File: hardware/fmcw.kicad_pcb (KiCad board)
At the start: 4 copper layers, 147.8 x 58.9 mm, 412 parts, among them CON1 BARREL_JACK, J1 SD_Card, J2 USB_B_Micro, J3 SMA, J4 SMA, J5 SMA, P1 CONN_02X04, P2 CONN_02X04, Q1 DNP(RE1C002UN), Q2 RE1C002UN, SW1 SW_PUSH, U1 LP5907MFX-3.3, U10 LP5907MFX-3.0, U11 LTC2292, U12 ADF4158, U13 TLV172DCK, U14 PAT1220-3dB, U15 HMC431LP4, U16 PD4859J5050S2HF, U17 PAT1220-5dB, U18 SE5004L, U19 DC4759J5020AHF, U2 LP5907MFX-1.8, U20 PAT1220-6dB, U22 TRF37A73, U23 SKY65404, U24 TRF37A73, U25 SKY65404, U26 TPS5420D, U27 TPS5420D, U28 TPS560200, U29 LP2985A-10DBVR, U3 KT2520K-T, U30 TPS7A7001DDA, U31 TPS7A91, U32 TPS7A91, U33 LP5907MFX-3.0, U34 TPS7A91, U35 5400BL15B050E, U36 5400BL15B050E, U37 5400BL15B050E, U38 ADL5802, U39 ADA4940-2, U4 NC7SVU04P5X, U5 NB3N551, U6 XC7A15T-FTG256, U7 W25Q32JV, U8 93LCxxB, U9 FT2232H, Y1 12MHz

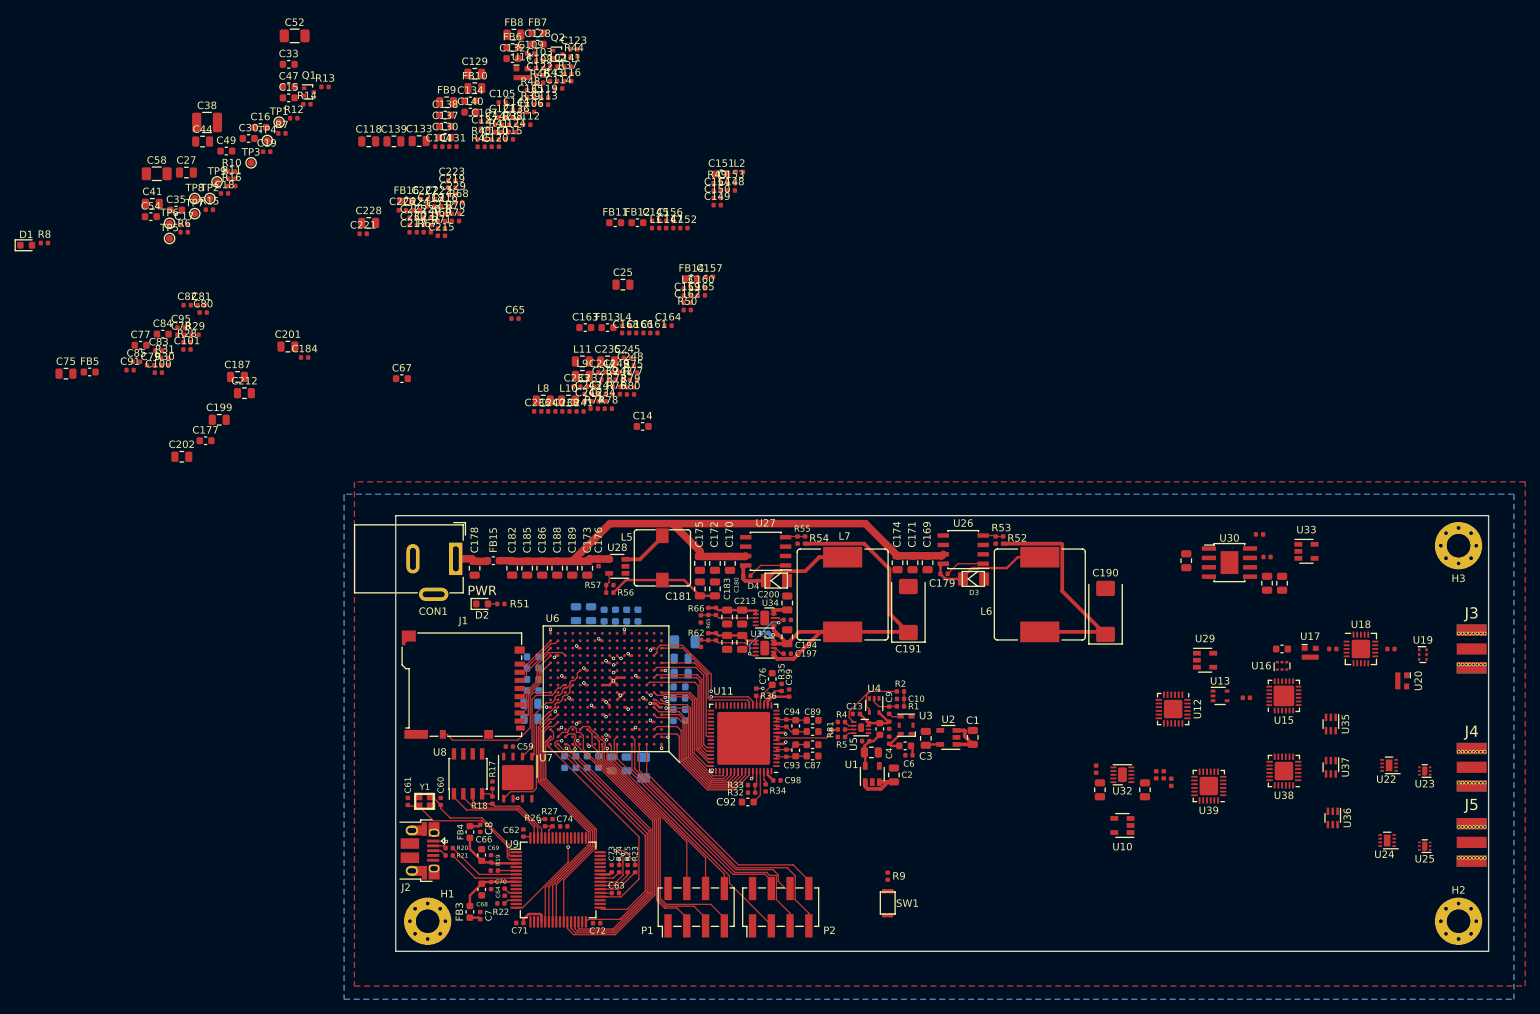
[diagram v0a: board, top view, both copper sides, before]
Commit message: Fixed transmission line width.
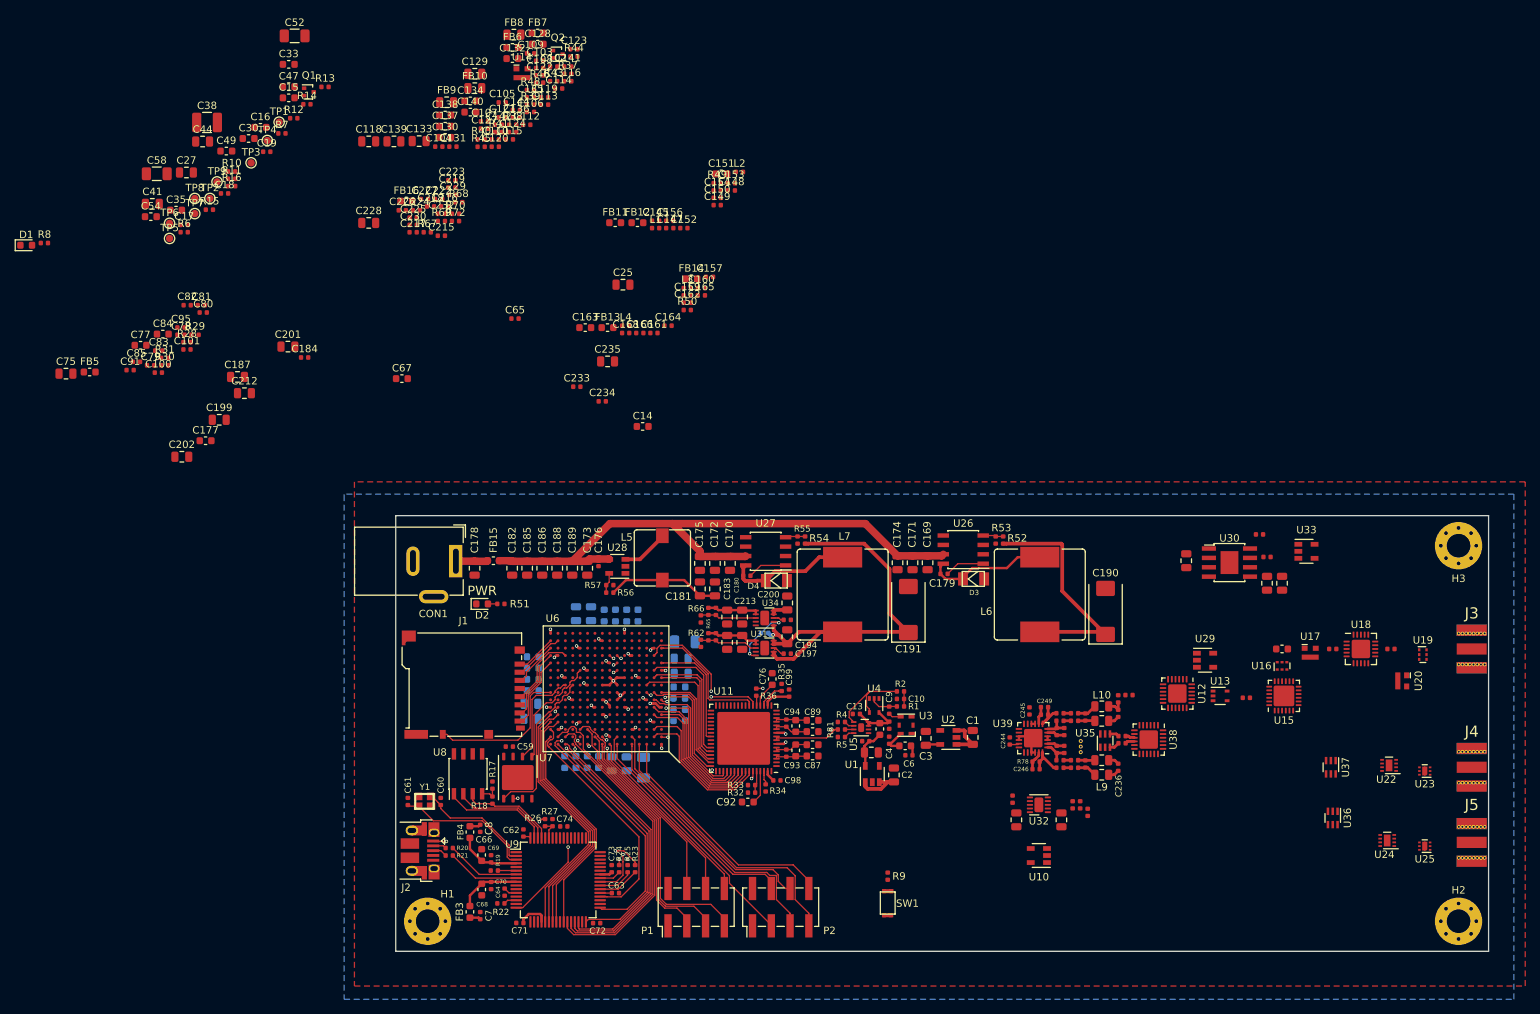
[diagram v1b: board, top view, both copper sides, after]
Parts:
- added REF**: RF_via, fmcw:RF_via, F.Cu at (179.0, 118.9)
- moved C221 123.6 mm to (184.6, 118.4), turned to 180 degrees
- moved C220 117.3 mm to (184.6, 117.4), turned to 180 degrees
- moved C231 114.3 mm to (185.5, 111.9), turned to 180 degrees
- moved R71 111.5 mm to (184.1, 112.4), turned to 90 degrees
- moved C236 92.1 mm to (184.1, 121.7), turned to 270 degrees
- moved L8 89.9 mm to (181.9, 120.7), turned to 180 degrees
- moved L9 88.6 mm to (181.9, 122.7), turned to 180 degrees
- moved L11 85.4 mm to (181.9, 115.4), turned to 180 degrees
- moved C240 85.0 mm to (178.2, 120.7)
- moved C238 84.9 mm to (179.6, 121.2), turned to 270 degrees
- moved C237 83.9 mm to (184.1, 114.4), turned to 270 degrees
- moved L10 83.2 mm to (181.9, 113.4), turned to 180 degrees
- moved C241 82.4 mm to (178.2, 121.7)
- moved R74 79.6 mm to (176.2, 121.7)
- moved C239 79.4 mm to (179.6, 114.9), turned to 270 degrees
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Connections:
- C236 pad 1: /if/IF1- -> /if/IF2-
- C236 pad 2: /if/IF1+ -> /if/IF2+
- C237 pad 1: /if/IF2+ -> /if/IF1-
- C237 pad 2: /if/IF2- -> /if/IF1+
- C244 pad 1: /ADC_VCM2 -> /ADC_VCM1
- C245 pad 1: /ADC_VCM1 -> /ADC_VCM2
- L10 pad 1: /if/IF2+ -> /if/IF1-
- L11 pad 1: /if/IF2- -> /if/IF1+
- L8 pad 1: /if/IF1- -> /if/IF2-
- L9 pad 1: /if/IF1+ -> /if/IF2+
- U39 pad 11: /ADC_VCM1 -> /ADC_VCM2
- U39 pad 12: /ADC2+ -> /ADC1-
- U39 pad 13: /ADC2- -> /ADC1+
- U39 pad 17: /ADC_VCM2 -> /ADC_VCM1
- U39 pad 18: /ADC1+ -> /ADC2+
- U39 pad 19: /ADC1- -> /ADC2-
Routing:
- net Net-(C246-Pad2): track 0.00 -> 5.47 mm
- net GND: track 23.9 -> 29.0 mm
- net Net-(C249-Pad1): track 0.00 -> 5.04 mm
- net Net-(C248-Pad1): track 0.00 -> 3.56 mm
- net Net-(C247-Pad2): track 0.00 -> 3.30 mm
- net Net-(C238-Pad2): track 0.00 -> 2.67 mm
- net Net-(C239-Pad1): track 0.00 -> 2.67 mm
- net Net-(C246-Pad1): track 0.00 -> 2.63 mm
- net /if/IF1-: track 0.00 -> 2.48 mm
- net Net-(C247-Pad1): track 0.00 -> 2.40 mm
- net Net-(C249-Pad2): track 0.00 -> 2.37 mm
- net Net-(C248-Pad2): track 0.00 -> 2.37 mm
- net Net-(C239-Pad2): track 0.00 -> 2.28 mm
- net Net-(C238-Pad1): track 0.00 -> 2.28 mm
- net /if/IF2+: track 0.00 -> 1.50 mm
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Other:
- net class RF_50: trace_width 0.304292 -> 0.379984

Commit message: Added test points.
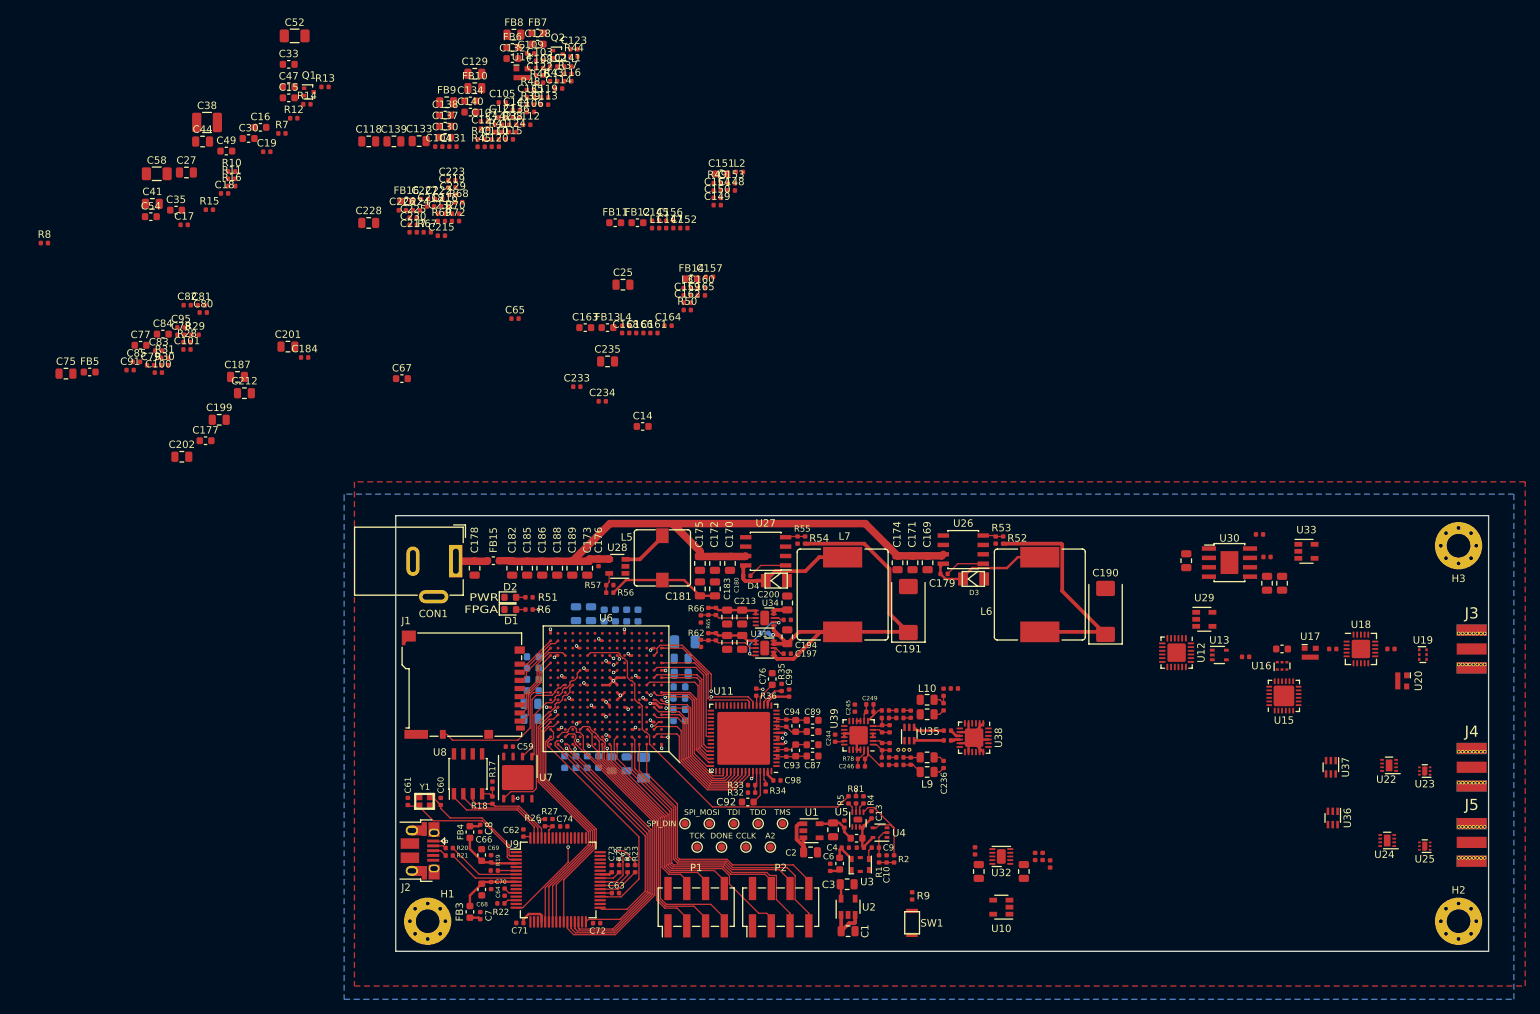
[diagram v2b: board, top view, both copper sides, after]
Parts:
- moved TP9 117.0 mm to (137.0, 132.5)
- moved TP8 115.1 mm to (133.7, 132.5)
- moved TP5 114.6 mm to (138.7, 129.3)
- moved TP4 113.8 mm to (135.4, 129.3)
- moved TP7 111.4 mm to (130.4, 132.5)
- moved TP3 110.7 mm to (132.1, 129.3)
- moved TP6 110.5 mm to (127.1, 132.5)
- moved TP1 109.6 mm to (125.5, 129.3)
- moved TP2 108.2 mm to (128.8, 129.3)
- moved D1 81.9 mm to (101.9, 100.3)
- moved R6 69.1 mm to (104.4, 100.3), turned to 180 degrees
- moved C1 31.2 mm to (147.5, 143.8), turned to 0 degrees
- moved U2 26.6 mm to (147.5, 140.5), turned to 90 degrees
- moved U35 26.5 mm to (155.8, 117.2)
- moved REF** 23.9 mm to (155.1, 119.3), turned to 180 degrees
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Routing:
- net /FPGA_REF: track 0.00 -> 49.8 mm
- net /fpga/LED: track 0.00 -> 27.3 mm, vias 0 -> 2
- net GND: track 29.0 -> 47.3 mm
- net /fpga/EXT2_1: track 34.5 -> 39.2 mm
- net /fpga/EXT2_2: track 36.5 -> 40.7 mm
- net /fpga/EXT2_6: track 32.9 -> 37.2 mm
- net /fpga/EXT2_5: track 32.7 -> 36.9 mm
- net /fpga/EXT2_4: track 30.7 -> 34.9 mm
- net /fpga/EXT2_3: track 38.1 -> 42.2 mm
- net /fpga/EXT1_6: track 25.9 -> 29.4 mm
- net Net-(C220-Pad2): track 1.27 -> 4.20 mm
- net Net-(C221-Pad2): track 1.38 -> 4.04 mm
- net /ADC_REF: track 22.3 -> 24.9 mm, vias 2 -> 3
- net /fpga/EXT1_5: track 26.4 -> 28.6 mm
- net Net-(C239-Pad1): track 2.67 -> 0.99 mm
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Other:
- board text added: "A2"
- board text added: "CCLK"
- board text added: "DONE"
- board text added: "FPGA"
- board text added: "SPI_DIN"
- board text added: "SPI_MOSI"
- board text added: "TCK"
- board text added: "TDI"
- board text added: "TDO"
- board text added: "TMS"

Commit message: Completed FPGA bypassing.
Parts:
- removed REF**: RF_via, fmcw:RF_via
- added F1: Via-fmcw3-rescue, fmcw:RF_via, F.Cu at (154.3, 109.3)
- added F2: Via-fmcw3-rescue, fmcw:RF_via, F.Cu at (155.2, 119.3)
- C14, C25, C27, C30, C33, C35, C38, C41, C44, C47, C49, C52, C54, C58: moved to B.Cu
- moved C52 104.7 mm to (106.2, 121.9), turned to 270 degrees
- moved C38 103.3 mm to (132.5, 108.8), turned to 90 degrees
- moved C41 99.6 mm to (129.8, 109.5), turned to 90 degrees
- moved C44 99.0 mm to (127.8, 109.5), turned to 90 degrees
- moved C47 98.0 mm to (124.8, 112.0)
- moved C49 94.8 mm to (124.8, 110.5)
- moved C54 92.1 mm to (108.1, 121.2), turned to 270 degrees
- moved C58 88.5 mm to (104.0, 114.4), turned to 180 degrees
- moved C33 84.8 mm to (101.2, 106.2), turned to 180 degrees
- moved C19 84.1 mm to (91.6, 119.4), turned to 270 degrees
- moved C30 77.4 mm to (104.6, 103.9), turned to 180 degrees
- moved C27 76.7 mm to (104.6, 102.1), turned to 180 degrees
- moved C35 76.1 mm to (104.6, 105.4), turned to 180 degrees
- moved C25 54.5 mm to (101.7, 108.7), turned to 270 degrees
- moved C14 34.8 mm to (104.6, 106.9)
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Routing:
- net /3V3D: track 17.6 -> 143.7 mm, vias 2 -> 16
- net /1V8: track 7.33 -> 53.4 mm, vias 0 -> 3
- net /1V0: track 15.3 -> 51.0 mm, vias 0 -> 4
- net /if/IF1-: track 2.48 -> 6.64 mm
- net Net-(C239-Pad1): track 0.99 -> 4.68 mm
- net Net-(C239-Pad2): track 0.99 -> 4.27 mm
- net /fpga/ADC_SHDN1: track 15.5 -> 18.1 mm
- net /if/IF1+: track 1.50 -> 4.16 mm
- net /FPGA_REF: track 49.8 -> 51.3 mm
- net GND: track 47.3 -> 48.6 mm, vias 29 -> 38
- net /LO: track 0.00 -> 1.18 mm
- net /MIX_ENBL: track 0.00 -> 1.18 mm, vias 0 -> 1
- net /fpga/TDI: track 28.6 -> 29.5 mm
- net /fpga/FT_D0: track 32.2 -> 31.4 mm
- net /fpga/LED: track 27.3 -> 27.9 mm
